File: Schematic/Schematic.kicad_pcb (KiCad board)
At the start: 2 copper layers, 115.1 x 171.2 mm, 134 parts, among them J1 HUB75_DATA, J10 Conn_01x03_Pin, J11 Conn_01x03_Pin, J12 Conn_01x03_Pin, J13 Conn_01x03_Pin, J14 Conn_01x03_Pin, J15 Conn_01x03_Pin, J16 Conn_01x03_Pin, J17 Conn_01x03_Pin, J18 LASER, J19 LDR, J2 KEYPAD, J20 WS2812B_DATA, J21 WS2812B_PWR, J3 HUB75_PWR, J4 AUDIO_OUT, J5 DEBUG_HEADER, J6 Conn_01x03_Pin, J7 Conn_01x03_Pin, J8 Conn_01x03_Pin, J9 Conn_01x03_Pin, SW1 RESET, U1 74LS08, U2 STM32F091RCT6, U3 LM386, U4 LM2678S-12, U5 LD1117S33TR_SOT223, U6 MAX7375AXR805, U7 LM358

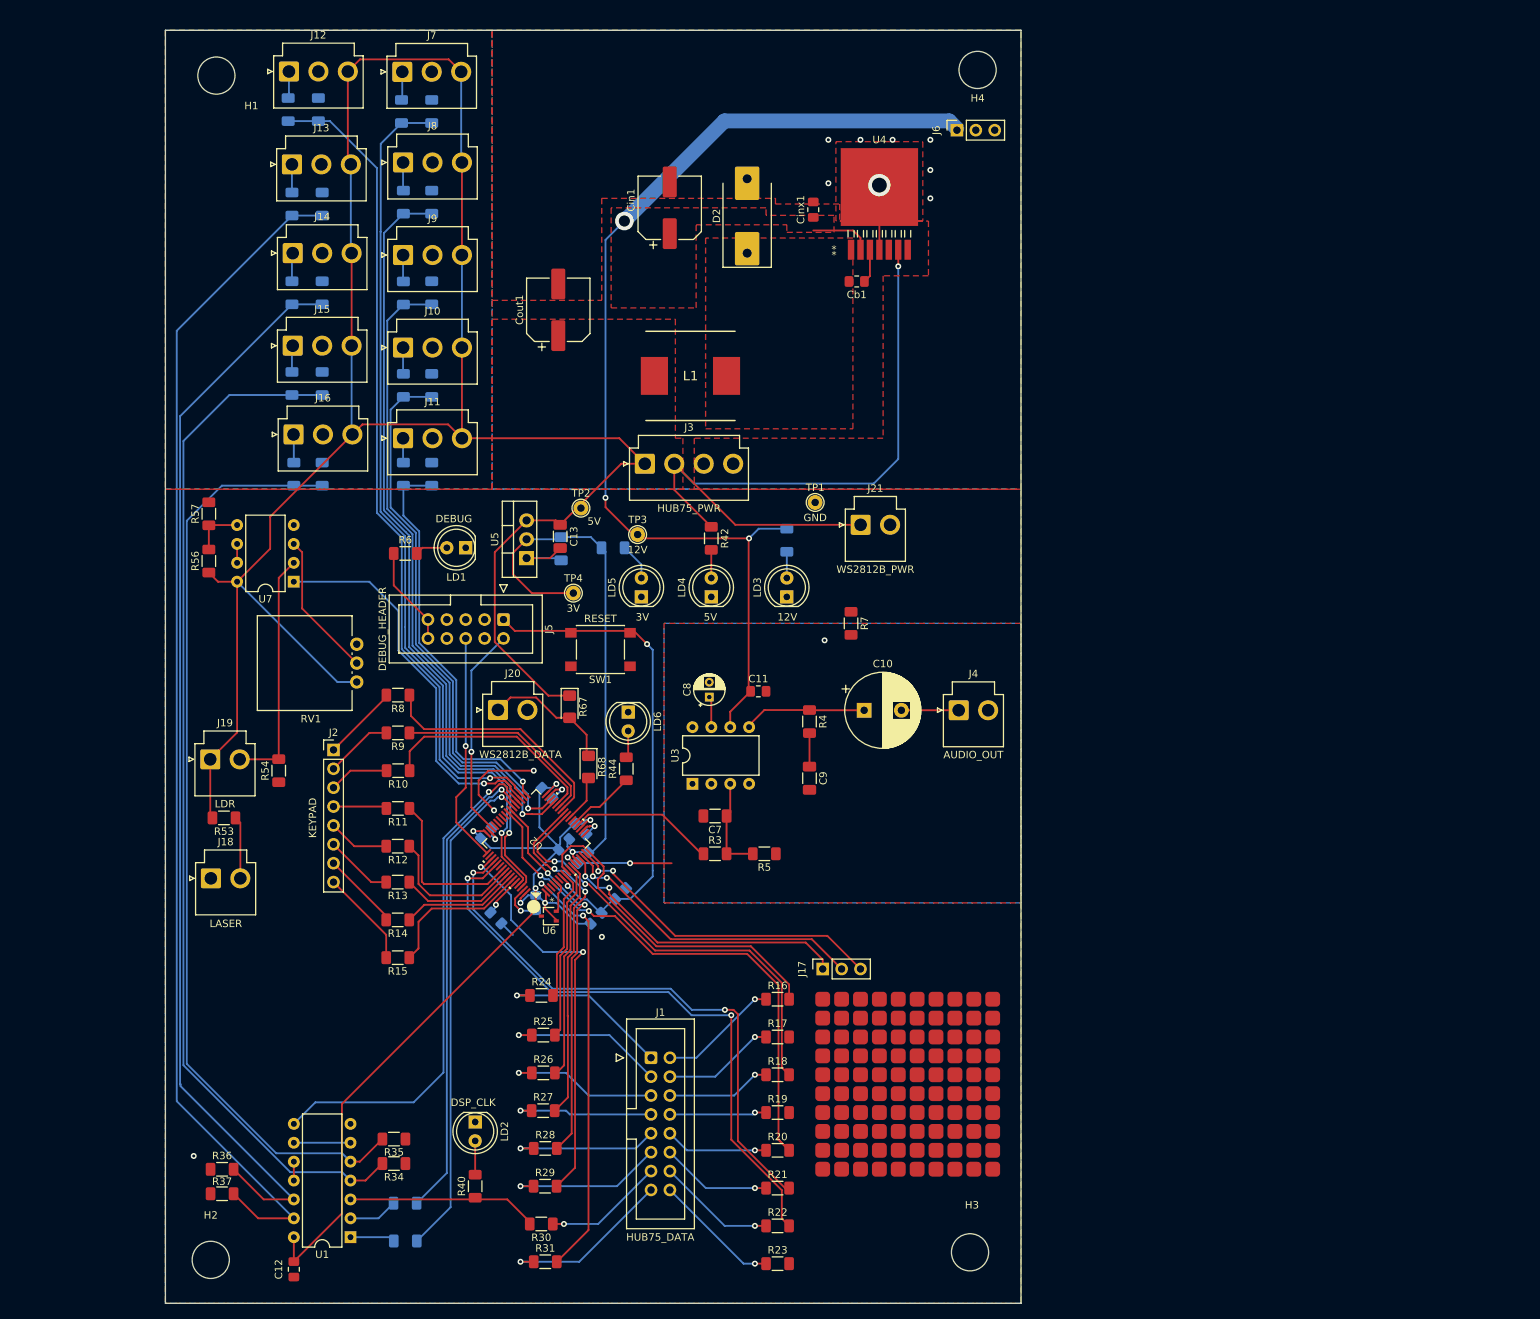
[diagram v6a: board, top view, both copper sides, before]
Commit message: Added images
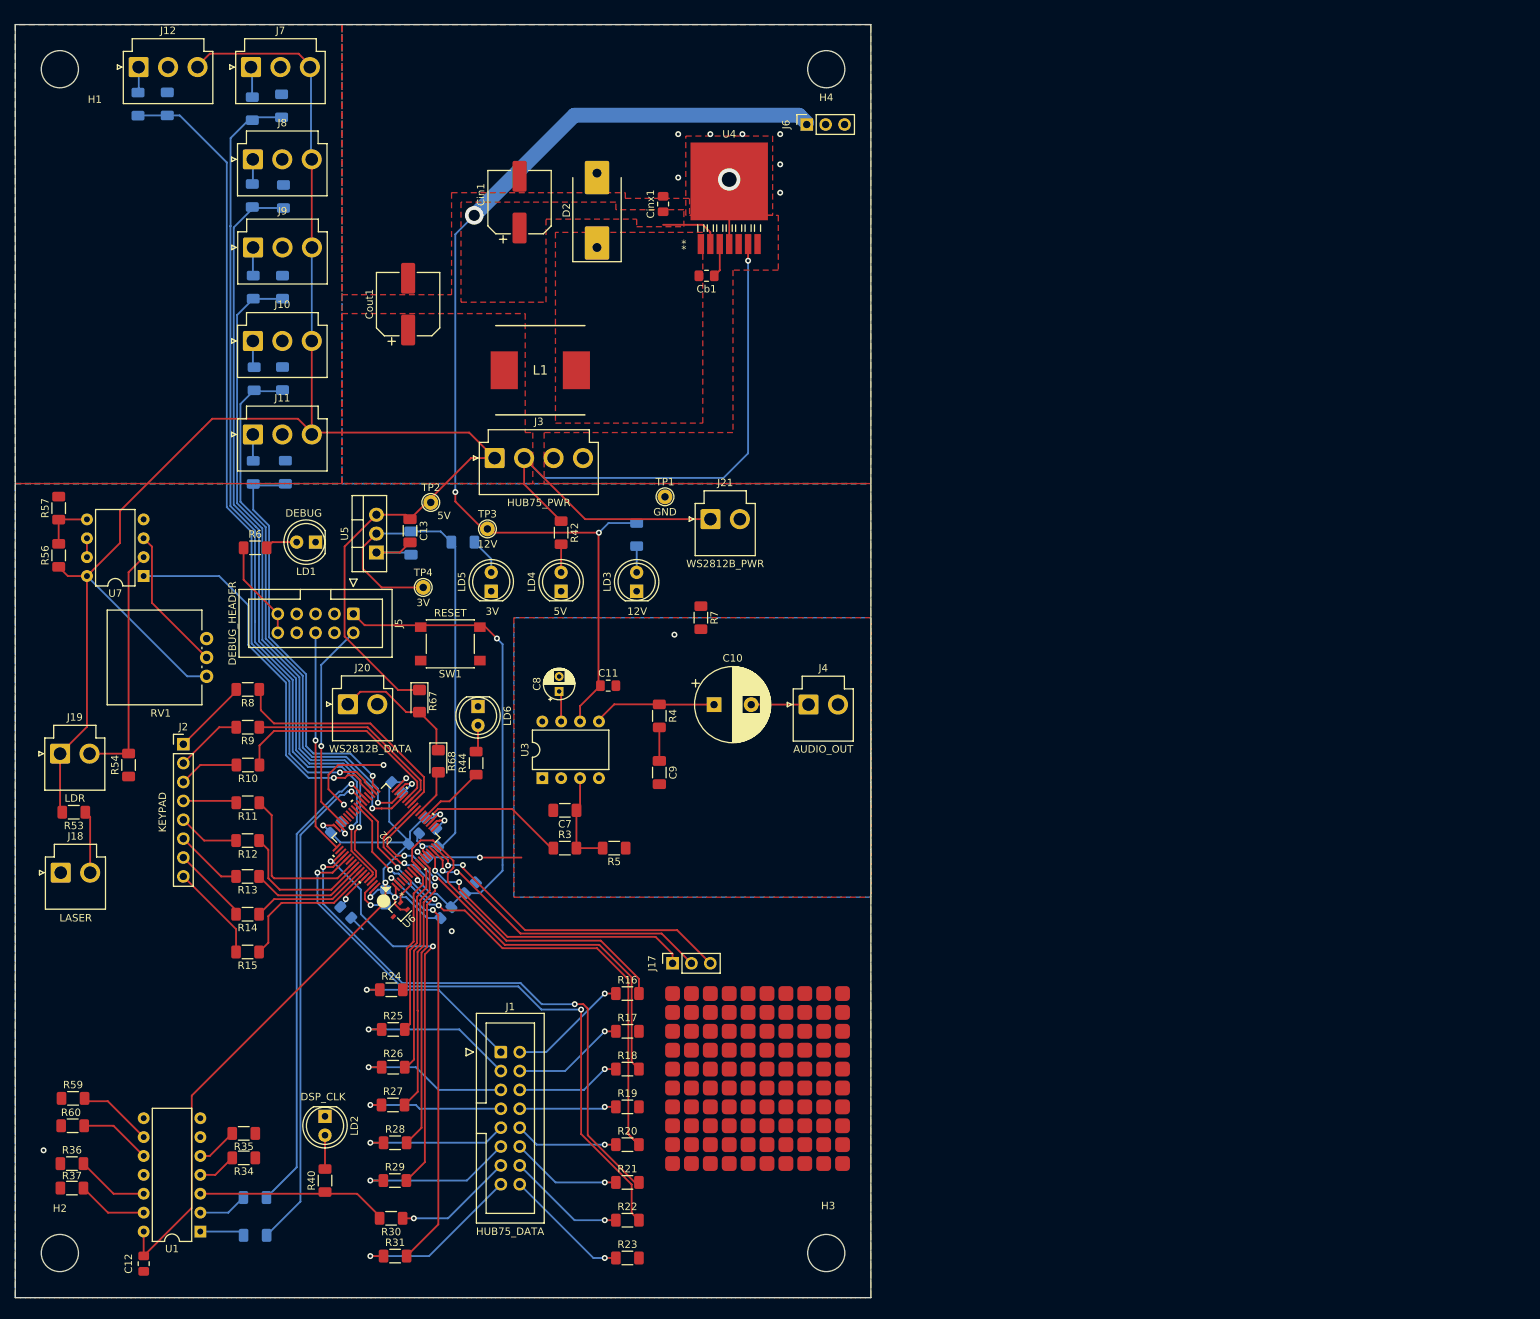
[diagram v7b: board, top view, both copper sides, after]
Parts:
- removed J13, J14, J15, J16: Conn_01x03_Pin, Connector_JST:JST_VH_B3P-VH_1x03_P3.96mm_Vertical
- removed R61, R62, R63, R64, R65, R66: 2k, Resistor_SMD:R_1206_3216Metric_Pad1.30x1.75mm_HandSolder
- R49, R50, R51, R52: value 1k -> 2k
- R5: value 20k -> 800
- R59, R60: value 2k -> 1k; moved to F.Cu
- moved R59 118.6 mm to (43.7, 168.0), turned to 0 degrees
- moved R60 110.7 mm to (43.7, 171.7), turned to 0 degrees
- moved R47 52.5 mm to (67.9, 83.8)
- moved R55 52.4 mm to (72.3, 83.8)
- moved R38 49.5 mm to (67.8, 34.9), turned to 90 degrees
- moved R48 38.0 mm to (52.5, 34.3)
- moved R58 37.9 mm to (56.4, 34.3)
- moved R52 36.2 mm to (71.9, 71.2)
- moved R50 30.1 mm to (72.0, 46.7)
- moved R49 30.0 mm to (71.8, 34.5)
- moved R51 29.9 mm to (71.9, 58.9)
- moved R39 25.8 mm to (67.8, 46.6), turned to 90 degrees
- moved H1 21.1 mm to (41.9, 29.6)
- moved J7 20.4 mm to (67.6, 29.3)
- moved H4 20.4 mm to (145.0, 29.6)
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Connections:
- R38 pad 1: Net-(J16-Pin_1) -> PB8
- R38 pad 2: Net-(R35-Pad2) -> Net-(J7-Pin_1)
- R39 pad 1: Net-(J15-Pin_1) -> PB9
- R39 pad 2: Net-(R34-Pad2) -> Net-(J8-Pin_1)
- R45 pad 1: Net-(J13-Pin_1) -> PB10
- R45 pad 2: Net-(R37-Pad2) -> Net-(J9-Pin_1)
- R46 pad 1: Net-(J14-Pin_1) -> PB11
- R46 pad 2: Net-(R36-Pad2) -> Net-(J10-Pin_1)
- R47 pad 1: PB8 -> PB12
- R47 pad 2: Net-(J7-Pin_1) -> Net-(J11-Pin_1)
- R48 pad 1: PB9 -> PB13
- R48 pad 2: Net-(J8-Pin_1) -> Net-(J12-Pin_1)
- R49 pad 1: PB10 -> PB8
- R49 pad 2: Net-(J9-Pin_1) -> GND
- R50 pad 1: PB11 -> PB9
- R50 pad 2: Net-(J10-Pin_1) -> GND
- R51 pad 1: PB12 -> PB10
- R51 pad 2: Net-(J11-Pin_1) -> GND
- R52 pad 1: PB13 -> PB11
- R52 pad 2: Net-(J12-Pin_1) -> GND
- R55 pad 1: PB8 -> PB12
- R58 pad 1: PB9 -> PB13
- R59 pad 1: PB10 -> GND
- R59 pad 2: GND -> Net-(R59-Pad2)
- R60 pad 1: PB11 -> GND
- R60 pad 2: GND -> Net-(R60-Pad2)
- U1 pad 10: Net-(U1-Pad10) -> Net-(R60-Pad2)
- U1 pad 11: Net-(U1-Pad10) -> unconnected-(U1-Pad11)
- U1 pad 6: Net-(U1-Pad6) -> unconnected-(U1-Pad6)
- U1 pad 8: PB15 -> unconnected-(U1-Pad8)
- U1 pad 9: Net-(U1-Pad6) -> Net-(R59-Pad2)
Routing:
- net Net-(R37-Pad2): track 161.3 -> 9.47 mm
- net Net-(R36-Pad2): track 146.8 -> 9.78 mm
- net Net-(R34-Pad2): track 139.3 -> 5.24 mm
- net Net-(R35-Pad2): track 126.2 -> 5.55 mm
- net PB15: track 68.9 -> 0.00 mm, vias 1 -> 0
- net +5V: track 394.2 -> 343.6 mm
- net Net-(R59-Pad2): track 0.00 -> 9.49 mm
- net Net-(R60-Pad2): track 0.00 -> 9.23 mm
- net Net-(U1-Pad6): track 7.62 -> 0.00 mm
- net Net-(J14-Pin_1): track 3.86 -> 0.00 mm
- net Net-(J16-Pin_1): track 3.80 -> 0.00 mm
- net Net-(J13-Pin_1): track 3.78 -> 0.00 mm
- net Net-(J15-Pin_1): track 3.57 -> 0.00 mm
- net Net-(U1-Pad10): track 2.54 -> 0.00 mm
- net /microprocessor/SWCLK_IN: track 31.1 -> 30.0 mm
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
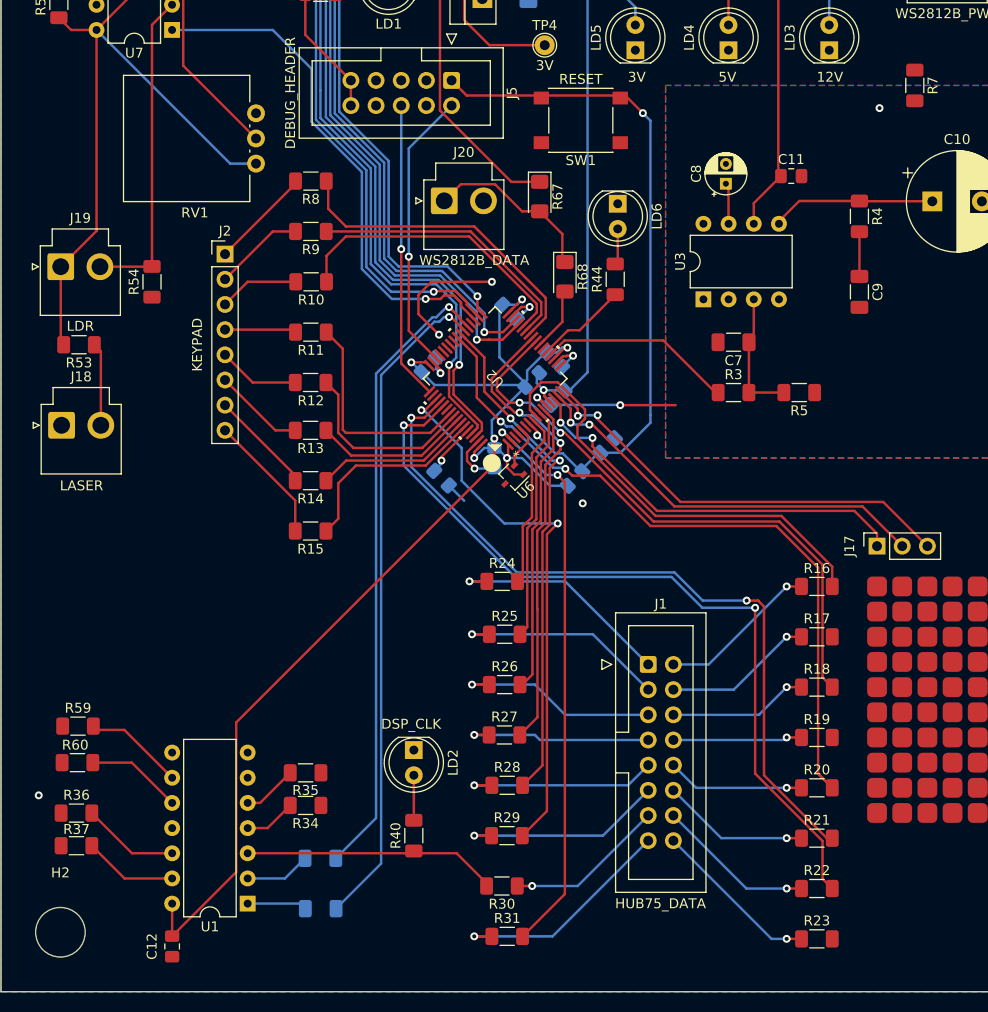
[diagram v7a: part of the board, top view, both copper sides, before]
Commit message: Added Cap to osilator, and fixed posible issues with signals near it.
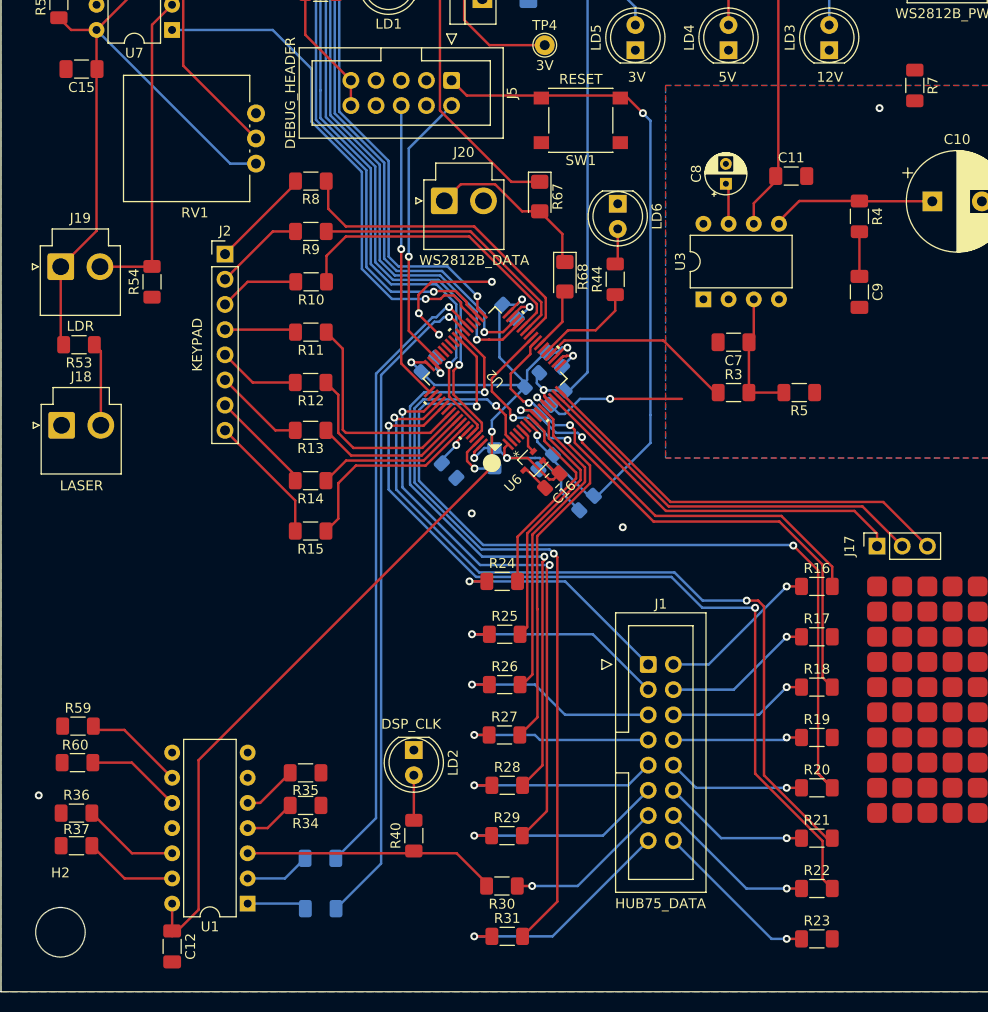
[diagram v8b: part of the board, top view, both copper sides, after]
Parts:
- added C15: 1u, Capacitor_SMD:C_1206_3216Metric_Pad1.33x1.80mm_HandSolder, F.Cu at (44.1, 101.7)
- added C16: .1uF, Capacitor_SMD:C_0805_2012Metric_Pad1.18x1.45mm_HandSolder, F.Cu at (91.6, 143.3)
- C11, C12: footprint Capacitor_SMD:C_0805_2012Metric_Pad1.18x1.45mm_HandSolder -> Capacitor_SMD:C_1206_3216Metric_Pad1.33x1.80mm_HandSolder
- moved C1 6.47 mm to (90.9, 141.4), turned to -135 degrees
- moved R1 2.74 mm to (95.0, 145.5)
- moved U6 2.36 mm to (89.4, 141.5)
- moved R2 1.08 mm to (81.2, 142.2)
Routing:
- net PC13: track 57.3 -> 77.8 mm
- net PC9: track 73.4 -> 89.8 mm
- net PC8: track 51.8 -> 63.4 mm
- net +3V0: track 127.9 -> 137.4 mm
- net PC11: track 76.5 -> 81.3 mm
- net PC12: track 81.8 -> 86.3 mm
- net PC1: track 46.0 -> 42.1 mm, vias 0 -> 2
- net /microprocessor/NRST: track 68.7 -> 72.6 mm
- net PC5: track 47.4 -> 50.8 mm
- net PC10: track 55.4 -> 58.2 mm
- net PC0: track 17.9 -> 20.6 mm
- net PC2: track 23.9 -> 26.6 mm
- net PC3: track 29.7 -> 32.4 mm
- net Net-(U2-PF0-OSC_IN): track 4.35 -> 2.61 mm
- net GNDA: track 15.6 -> 17.2 mm
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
